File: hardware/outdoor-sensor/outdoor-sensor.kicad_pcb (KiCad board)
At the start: 2 copper layers, 11 parts, among them J1 POWER, J2 UART, SW1 RESET, SW2 BOOT, U1 ESP32-WROOM-32, U2 DS18B20

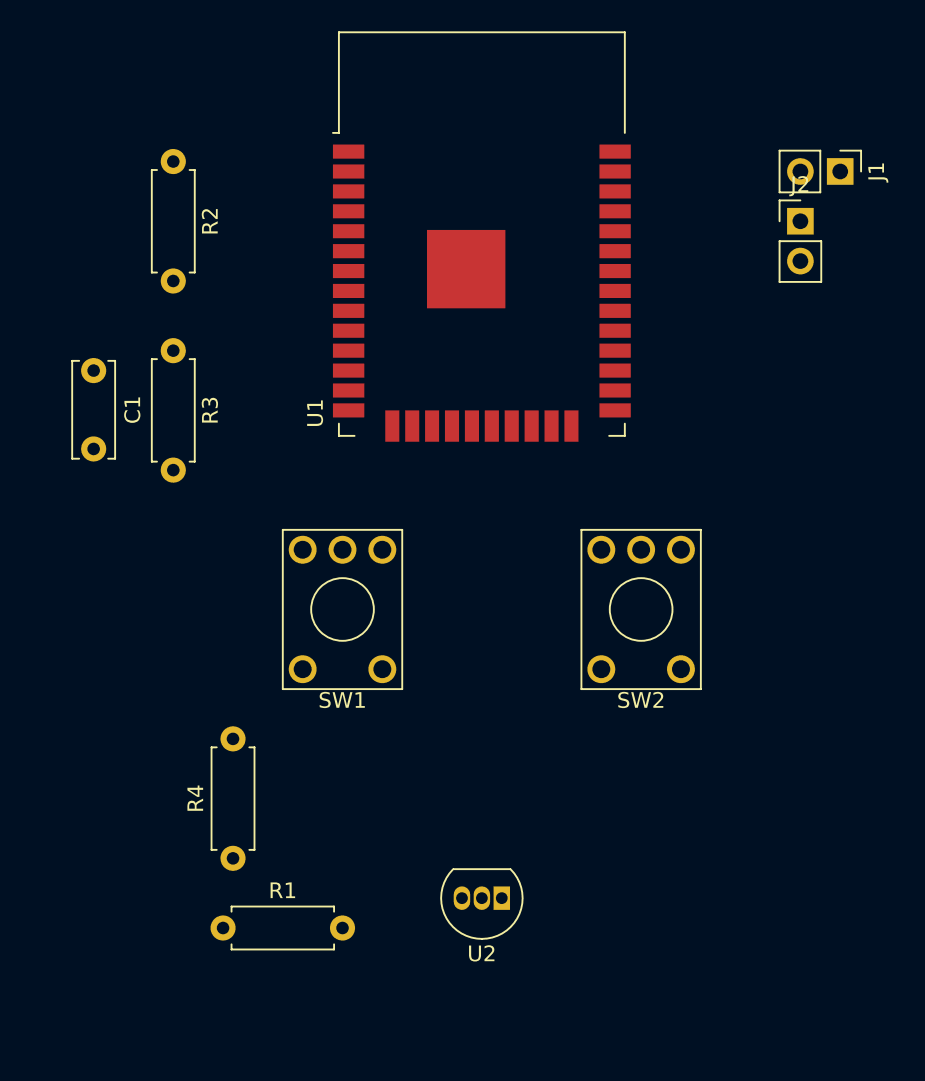
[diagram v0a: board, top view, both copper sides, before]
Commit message: Swap out DS18B20 for DS18B20-PAR
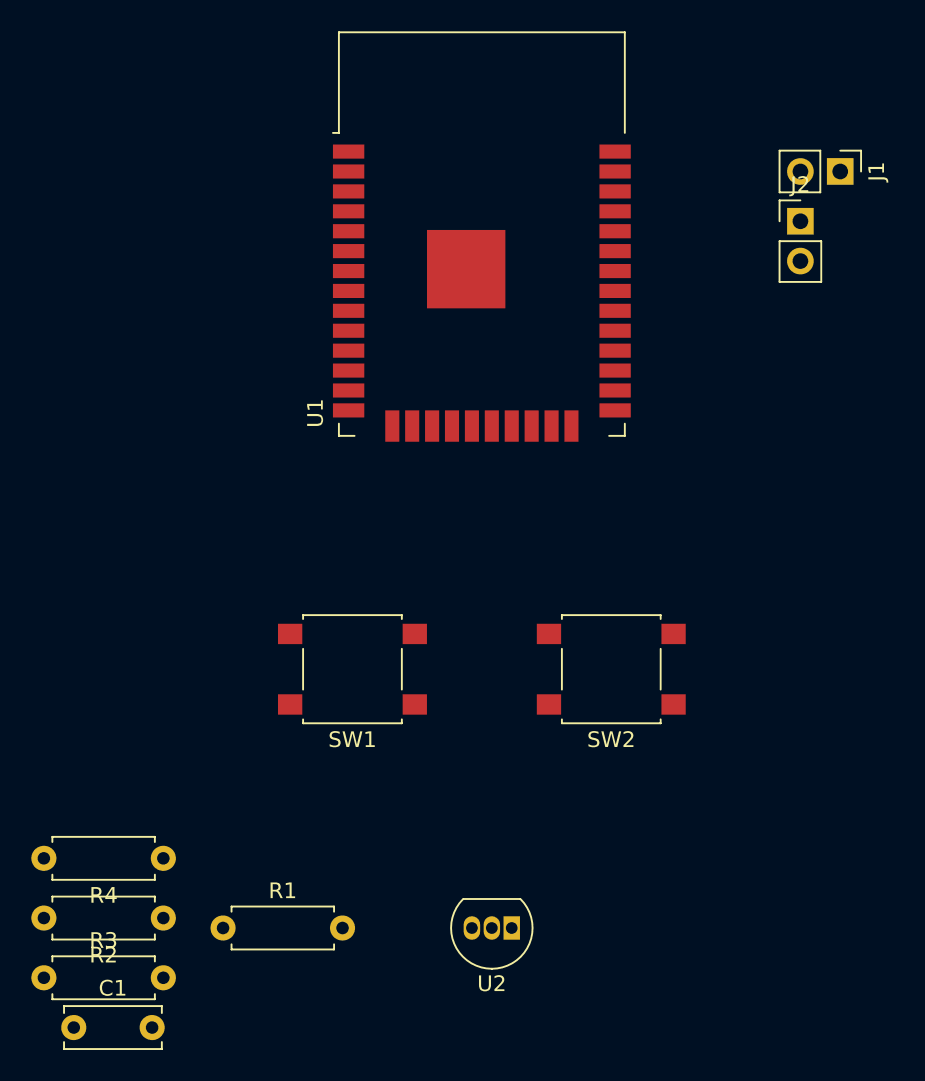
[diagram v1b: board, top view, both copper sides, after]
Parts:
- SW1, SW2: footprint Button_Switch_THT:KSA_Tactile_SPST -> Button_Switch_SMD:SW_SPST_B3S-1000
- U2: value DS18B20 -> DS18B20-PAR
- moved R2 48.3 mm to (80.0, 73.7), turned to 180 degrees
- moved C1 41.9 mm to (74.3, 80.6), turned to 0 degrees
- moved R3 40.8 mm to (72.4, 77.5), turned to 0 degrees
- moved SW2 4.45 mm to (108.6, 57.8)
- moved R4 4.44 mm to (80.0, 69.8), turned to 180 degrees
- moved U2 2.01 mm to (102.2, 74.3)
- moved SW1 1.91 mm to (92.1, 57.8)
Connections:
- U2 pad 3: +3V3 -> Net-(U2-Pad3)
